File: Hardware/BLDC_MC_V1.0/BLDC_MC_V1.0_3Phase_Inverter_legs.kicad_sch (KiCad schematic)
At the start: 18 parts, among them Q1 BSC0702LS, Q2 BSC0702LS, Q3 BSC0702LS, Q4 BSC0702LS, Q5 BSC0702LS, Q6 BSC0702LS

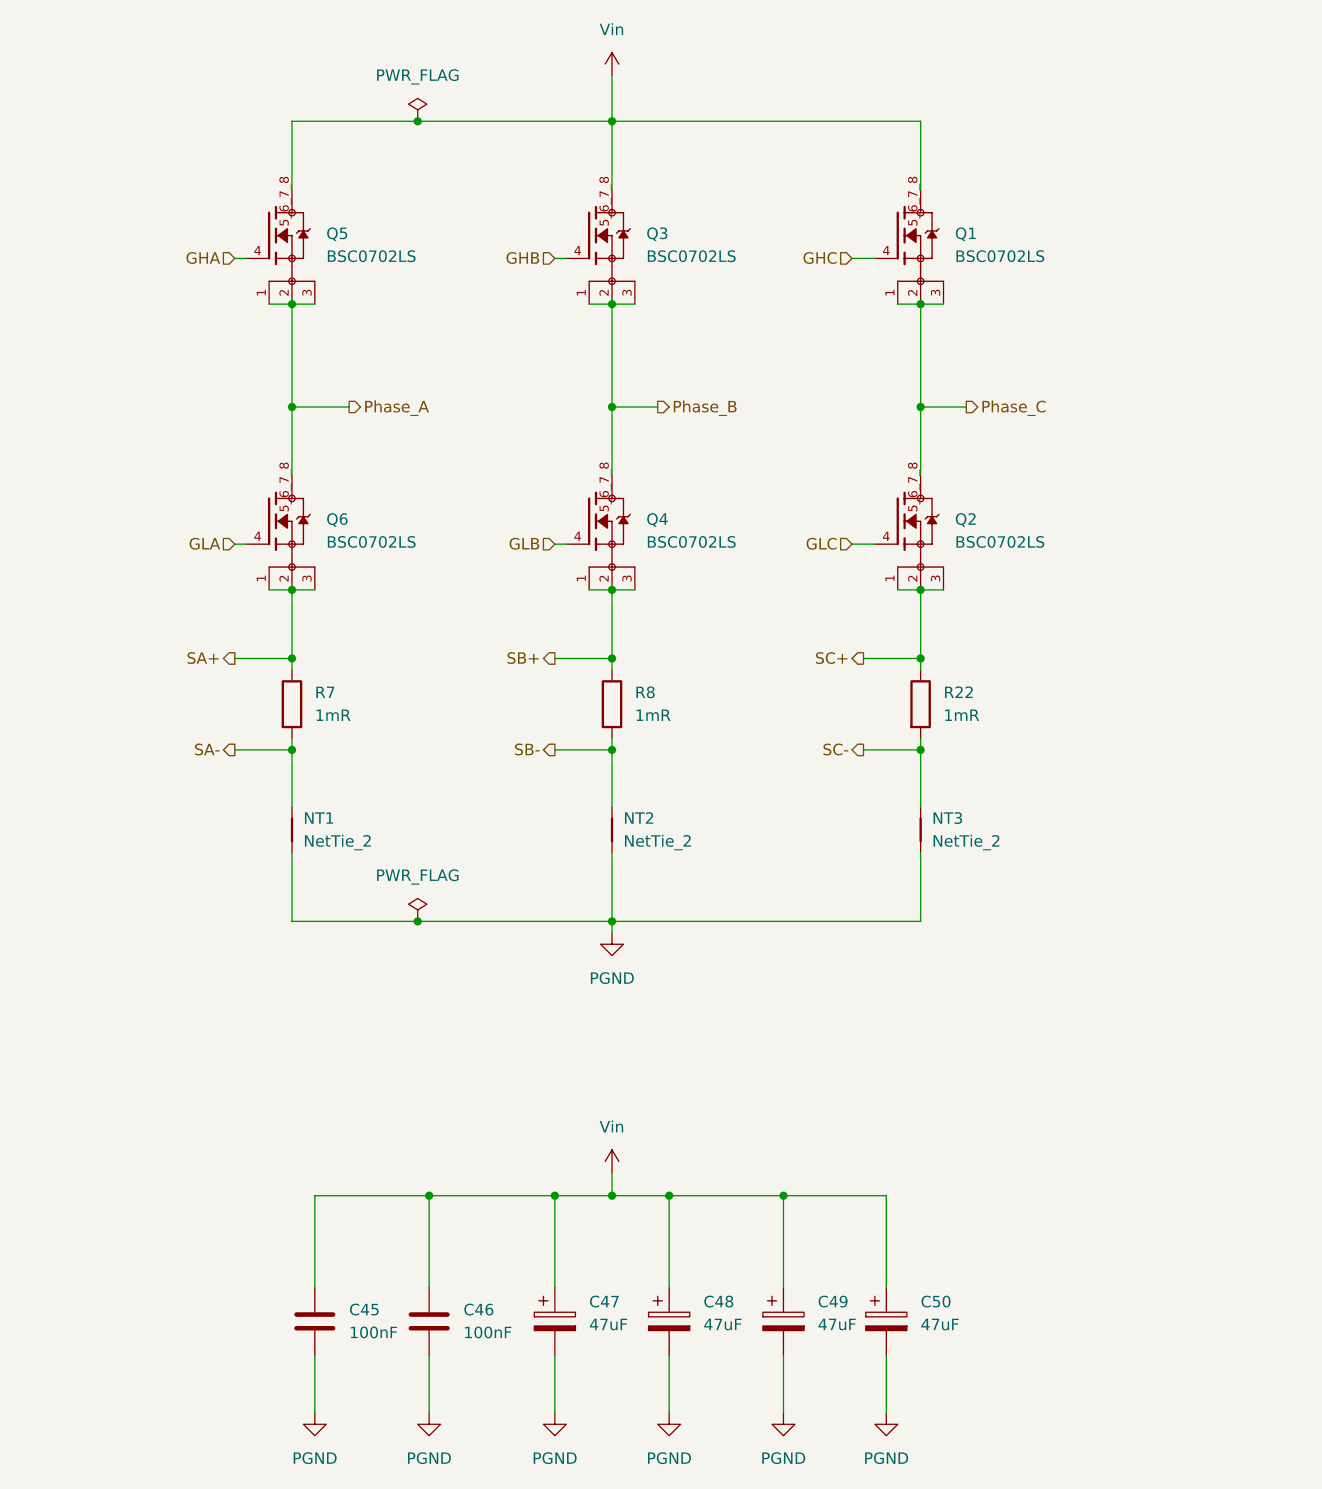
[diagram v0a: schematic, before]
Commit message: Add snubber circuit and edit pages numbers
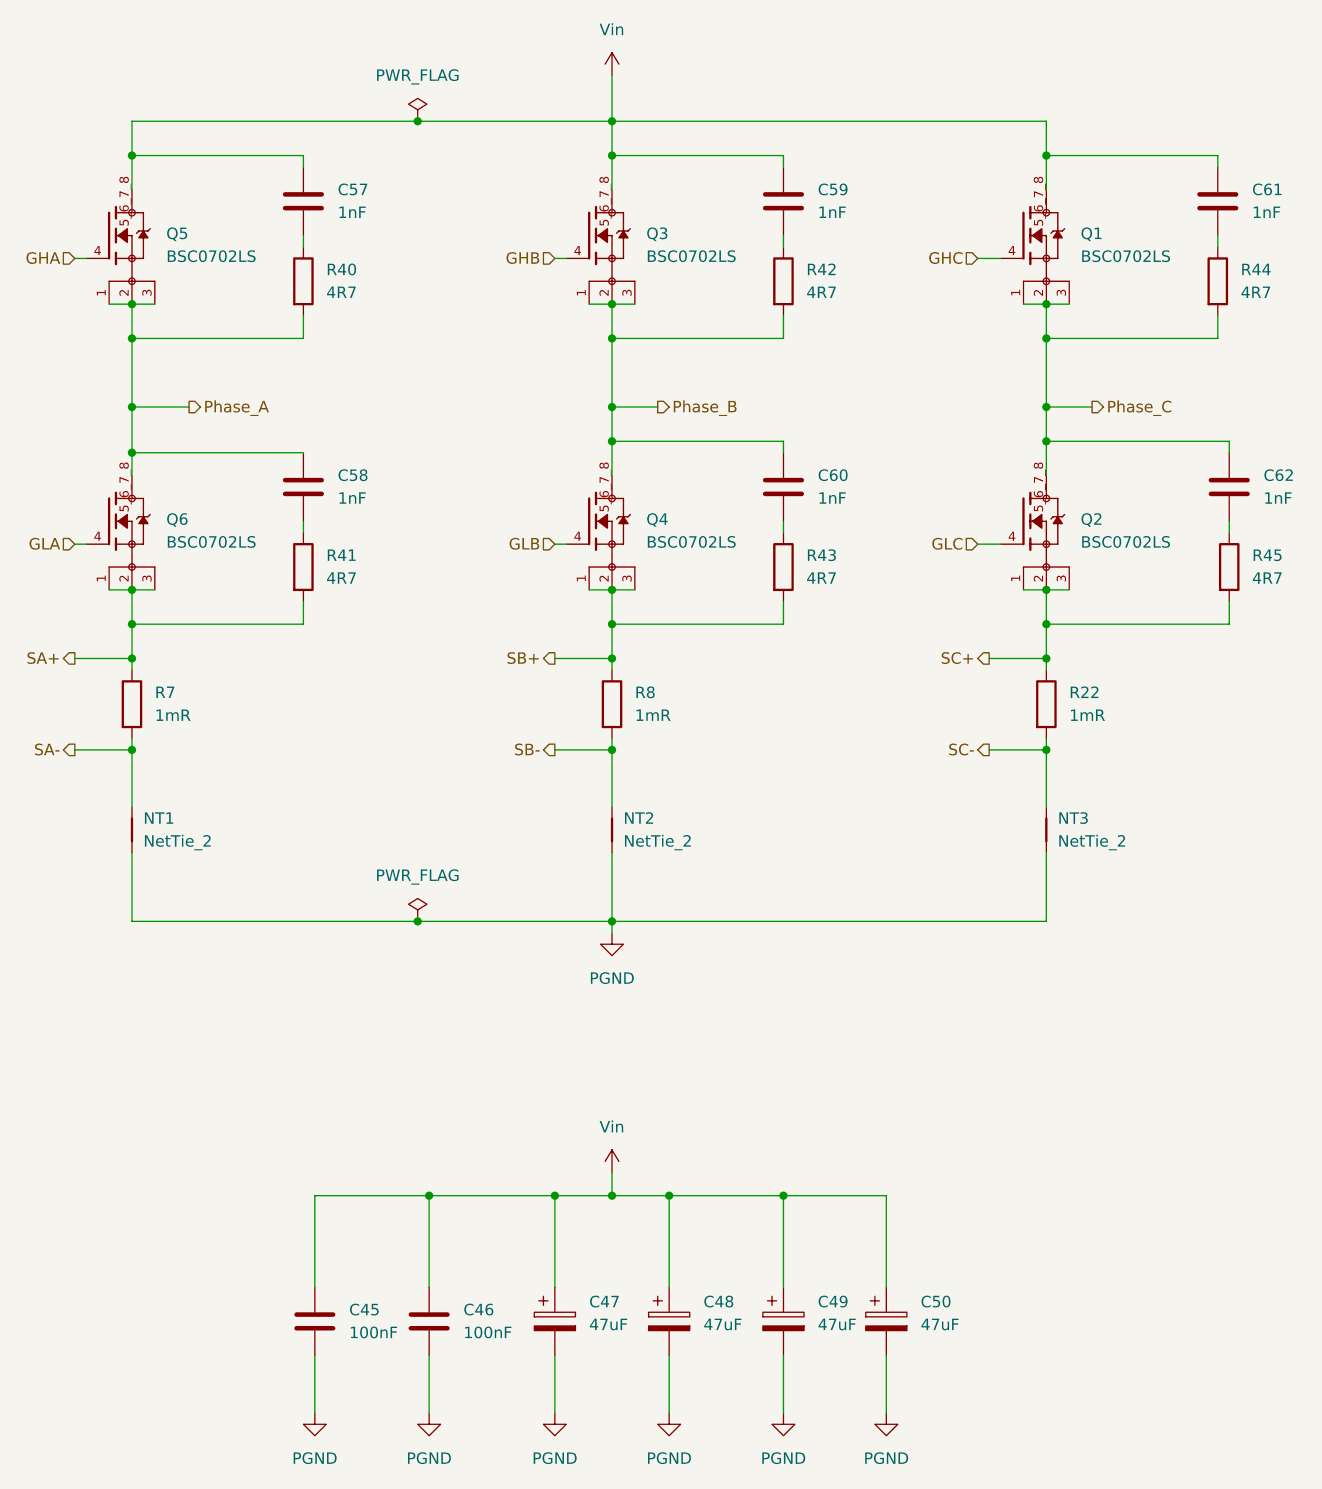
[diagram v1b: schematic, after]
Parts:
- added C57, C58, C59, C60, C61, C62: 1nF, Capacitor_SMD:C_1206_3216Metric, symbol Device:C
- added R40, R41, R42, R43, R44, R45: 4R7, Resistor_SMD:R_2512_6332Metric_Pad1.40x3.35mm_HandSolder, symbol Device:R
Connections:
- net Phase_A: now also C58.1, R40.2
- net Phase_B: now also C60.1, R42.2
- net Phase_C: now also C62.1, R44.2
- net SA+: now also R41.2
- net SB+: now also R43.2
- net SC+: now also R45.2
- net Vin: now also C57.1, C59.1, C61.1
- new net: C62.2, R45.1
- new net: C61.2, R44.1
- new net: C57.2, R40.1
- new net: C59.2, R42.1
- new net: C58.2, R41.1
- new net: C60.2, R43.1
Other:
- moved on the sheet: NT1, NT3, Q1, Q2, Q5, Q6, R22, R7
